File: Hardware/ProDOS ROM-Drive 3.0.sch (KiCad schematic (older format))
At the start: 17 parts, among them J1 Apple II Expansion Slot, U1 74LS00, U2 74LS32

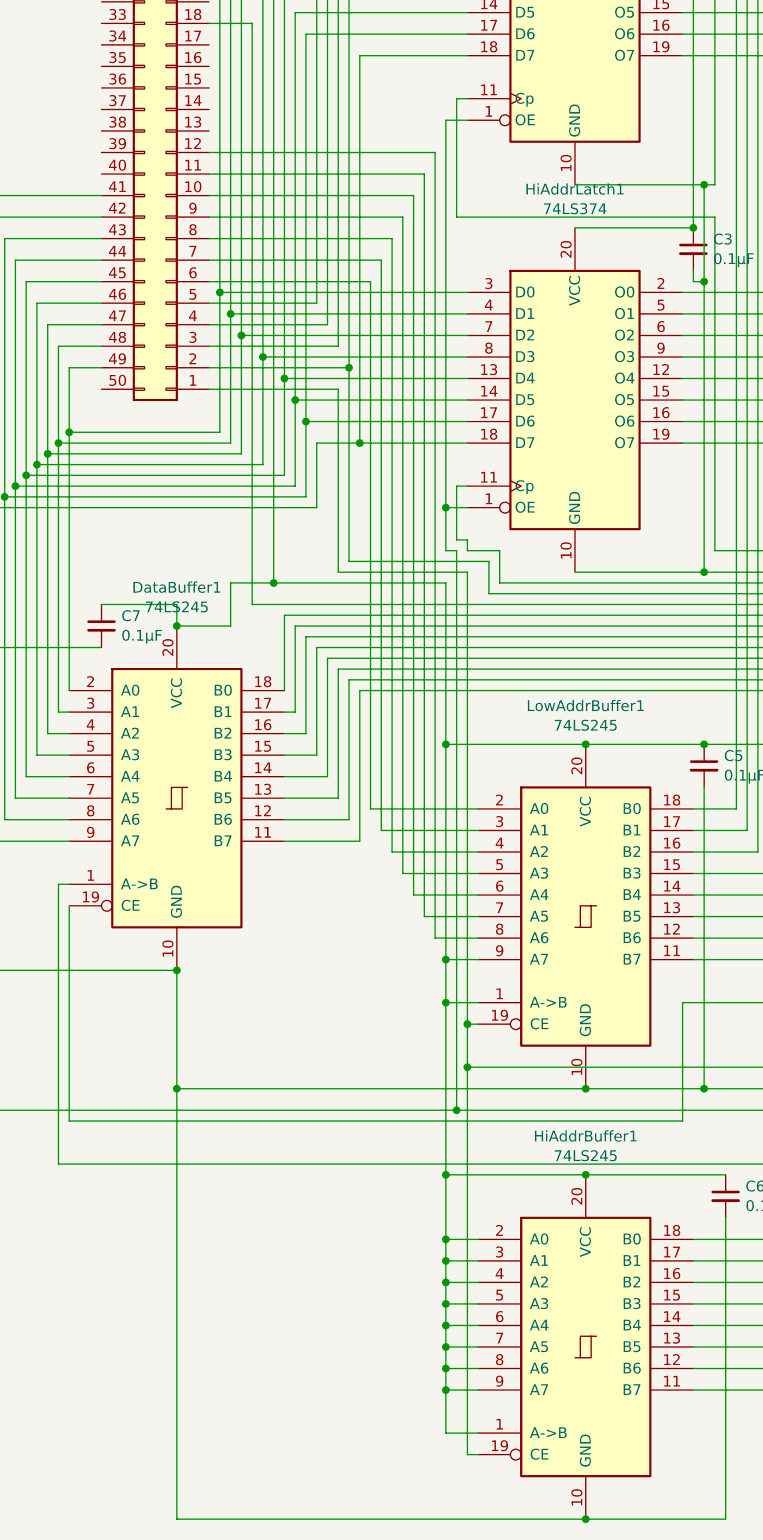
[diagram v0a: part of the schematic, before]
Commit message: Update hardware to use block 0001 for firmware
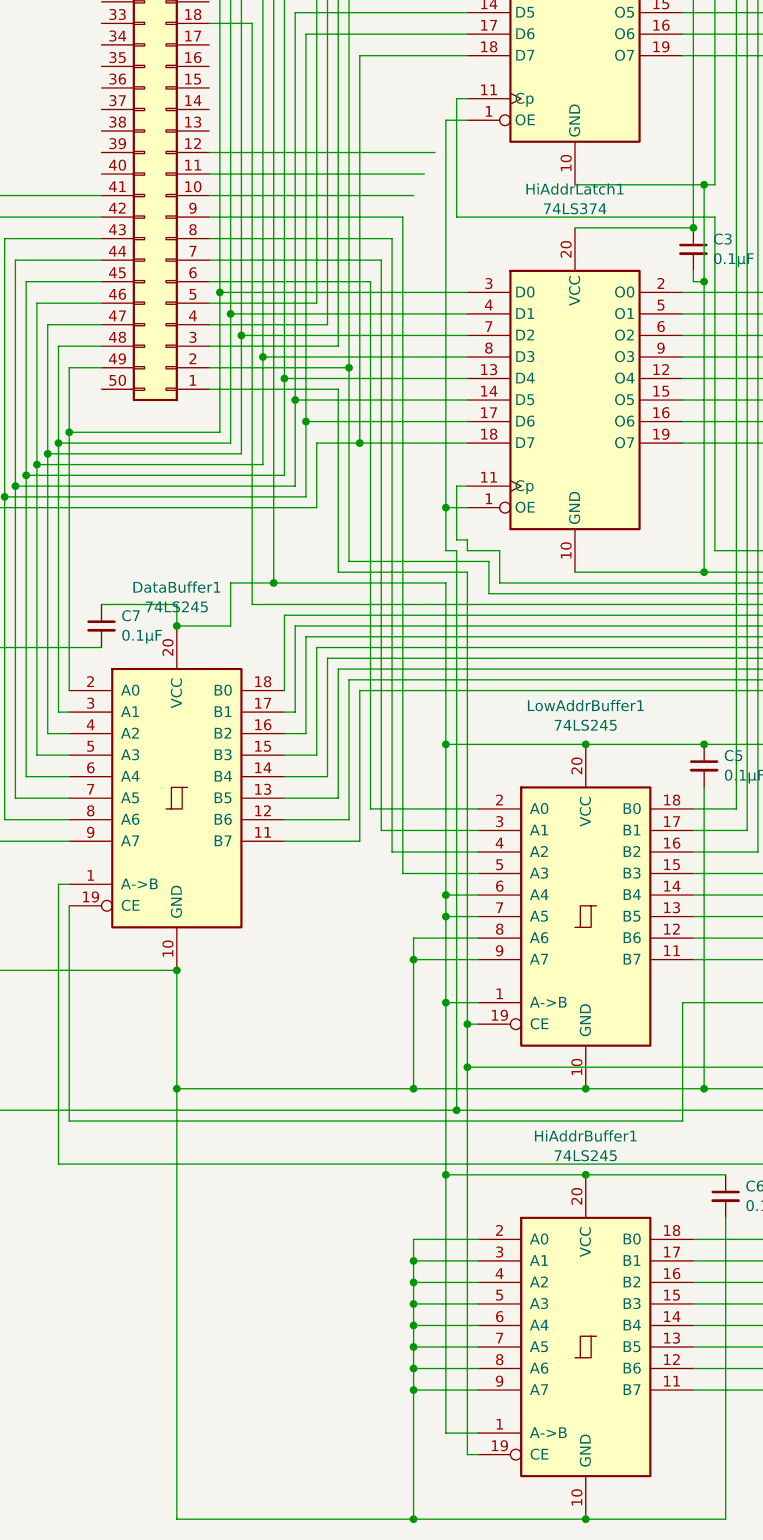
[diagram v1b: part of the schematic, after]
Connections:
- net +5V: now also LowAddrBuffer1.6 (A4), LowAddrBuffer1.7 (A5); no longer HiAddrBuffer1.2 (A0), HiAddrBuffer1.3 (A1), HiAddrBuffer1.4 (A2), HiAddrBuffer1.5 (A3), HiAddrBuffer1.6 (A4), HiAddrBuffer1.7 (A5), HiAddrBuffer1.8 (A6), HiAddrBuffer1.9 (A7), LowAddrBuffer1.9 (A7)
- net GND: now also HiAddrBuffer1.2 (A0), HiAddrBuffer1.3 (A1), HiAddrBuffer1.4 (A2), HiAddrBuffer1.5 (A3), HiAddrBuffer1.6 (A4), HiAddrBuffer1.7 (A5), HiAddrBuffer1.8 (A6), HiAddrBuffer1.9 (A7), LowAddrBuffer1.8 (A6), LowAddrBuffer1.9 (A7)
- net at J1.10 (Pin_10): no longer LowAddrBuffer1.6 (A4)
- net at J1.11 (Pin_11): no longer LowAddrBuffer1.7 (A5)
- net at J1.12 (Pin_12): no longer LowAddrBuffer1.8 (A6)
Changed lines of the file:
@@
 EESchema Schematic File Version 4
-LIBS:ProDOS ROMDrive 2-cache
-EELAYER 26 0
+EELAYER 30 0
 EELAYER END
 $Descr USLetter 8500 11000 portrait
@@
 Sheet 1 1
 Title "ProDOS ROM-Drive"
-Date ""
-Rev "2.2"
+Date "2021-12-07"
+Rev "3.0"
 Comp ""
 Comment1 ""
@@
 	1800 2950 2750 2950
 Wire Wire Line
-	2750 2950 2750 6200
-Wire Wire Line
-	2750 6200 3050 6200
-Wire Wire Line
 	1800 2850 2800 2850
 Wire Wire Line
-	2800 2850 2800 6300
-Wire Wire Line
-	2800 6300 3050 6300
-Wire Wire Line
 	1800 2750 2850 2750
 Wire Wire Line
-	2850 2750 2850 6400
-Wire Wire Line
-	2850 6400 3050 6400
-Wire Wire Line
 	1800 1450 2100 1450
 Wire Wire Line
@@
 Wire Wire Line
 	2900 4750 2900 5500
-Wire Wire Line
-	2900 6500 3050 6500
-Wire Wire Line
-	2900 6500 2900 6700
-Wire Wire Line
-	2900 7800 3050 7800
-Connection ~ 2900 6500
-Wire Wire Line
-	2900 7800 2900 7900
-Wire Wire Line
-	2900 7900 3050 7900
-Connection ~ 2900 7800
-Wire Wire Line
-	2900 7900 2900 8000
-Wire Wire Line
-	2900 8000 3050 8000
-Connection ~ 2900 7900
-Wire Wire Line
-	2900 8000 2900 8100
-Wire Wire Line
-	2900 8100 3050 8100
-Connection ~ 2900 8000
-Wire Wire Line
-	2900 8100 2900 8200
-Wire Wire Line
-	2900 8200 3050 8200
-Connection ~ 2900 8100
-Wire Wire Line
-	2900 8200 2900 8300
-Wire Wire Line
-	2900 8300 3050 8300
-Connection ~ 2900 8200
-Wire Wire Line
-	2900 8300 2900 8400
-Wire Wire Line
-	2900 8400 3050 8400
-Connection ~ 2900 8300
-Wire Wire Line
-	2900 8400 2900 8500
-Wire Wire Line
-	2900 8500 3050 8500
-Connection ~ 2900 8400
 Wire Wire Line
 	3550 7500 2900 7500
 Connection ~ 2900 7500
 Wire Wire Line
-	2900 7500 2900 7800
-Wire Wire Line
 	3550 5500 2900 5500
 Connection ~ 2900 5500
 Wire Wire Line
-	2900 5500 2900 6500
+	2900 5500 2900 6200
 Wire Wire Line
 	2100 4750 1900 4750
@@
 	1650 6550 1650 7100
 Wire Wire Line
-	1650 7100 3550 7100
+	1650 7100 2750 7100
 Connection ~ 1650 6550
 Wire Wire Line
@@
 	1650 7100 1650 9100
 Wire Wire Line
-	1650 9100 3550 9100
+	1650 9100 2750 9100
 Connection ~ 1650 7100
 Wire Wire Line
@@
 Wire Wire Line
 	2400 4700 3000 4700
-Wire Wire Line
-	3000 4700 3000 6800
 Wire Wire Line
 	3000 7000 5250 7000
@@
 Wire Wire Line
 	3000 6800 3050 6800
-Connection ~ 3000 6800
 Wire Wire Line
 	3000 6800 3000 7000
@@
 	700  2950 700  7200
 Wire Wire Line
-	700  7200 2950 7200
-Wire Wire Line
-	2950 7200 2950 4600
-Connection ~ 2950 7200
-Wire Wire Line
-	2950 7200 5150 7200
-Wire Wire Line
 	2900 4400 2900 2600
 Wire Wire Line
@@
 	2900 6700 2900 7500
 Wire Wire Line
-	2900 8500 2900 8700
-Wire Wire Line
 	2900 8700 3050 8700
-Connection ~ 2900 8500
 Wire Wire Line
 	2450 3750 2450 4650
@@
 	6200 7350 6200 7550
 Connection ~ 6550 7100
+Wire Wire Line
+	2900 7500 2900 8700
+Wire Wire Line
+	2750 9100 2750 8500
+Wire Wire Line
+	2750 7800 3050 7800
+Connection ~ 2750 9100
+Wire Wire Line
+	2750 9100 3550 9100
+Wire Wire Line
+	3050 7900 2750 7900
+Connection ~ 2750 7900
+Wire Wire Line
+	2750 7900 2750 7800
+Wire Wire Line
+	3050 8000 2750 8000
+Connection ~ 2750 8000
+Wire Wire Line
+	2750 8000 2750 7900
+Wire Wire Line
+	3050 8100 2750 8100
+Connection ~ 2750 8100
+Wire Wire Line
+	2750 8100 2750 8000
+Wire Wire Line
+	3050 8200 2750 8200
+Connection ~ 2750 8200
+Wire Wire Line
+	2750 8200 2750 8100
+Wire Wire Line
+	3050 8300 2750 8300
+Connection ~ 2750 8300
+Wire Wire Line
+	2750 8300 2750 8200
+Wire Wire Line
+	3050 8400 2750 8400
+Connection ~ 2750 8400
+Wire Wire Line
+	2750 8400 2750 8300
+Wire Wire Line
+	3050 8500 2750 8500
+Connection ~ 2750 8500
+Wire Wire Line
+	2750 8500 2750 8400
+Wire Wire Line
+	2750 7100 2750 6500
+Connection ~ 2750 7100
+Wire Wire Line
+	2750 7100 3550 7100
+Wire Wire Line
+	3050 6400 2750 6400
+Wire Wire Line
+	3050 6300 2900 6300
+Connection ~ 2900 6300
+Connection ~ 3000 6800
+Wire Wire Line
+	3000 4700 3000 6800
+Wire Wire Line
+	2900 6300 2900 6700
+Wire Wire Line
+	2950 7200 5150 7200
+Wire Wire Line
+	700  7200 2950 7200
+Connection ~ 2950 7200
+Wire Wire Line
+	2950 7200 2950 4600
+Wire Wire Line
+	3050 6500 2750 6500
+Connection ~ 2750 6500
+Wire Wire Line
+	2750 6500 2750 6400
+Wire Wire Line
+	3050 6200 2900 6200
+Connection ~ 2900 6200
+Wire Wire Line
+	2900 6200 2900 6300
 $EndSCHEMATC
